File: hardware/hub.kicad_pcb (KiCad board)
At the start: 4 copper layers, 100 x 85 mm, 153 parts, among them J101 USB-A, J102 TNG-Power-BTM, J103 TNG-Power-TOP, J104 TNG-Data-BTM, J105 TNG-Data-TOP, P101 Debug, P102 PE, P202 PWR IN, SW101 BOOT, T201 744272251, U101 USB2517, U102 MIC2026-1YM, U103 82400152, U104 STM32F070CBT6, U105 TPD4S010DQA, U106 TPD4S010DQA, U107 TPD4S010DQA, U110 TPS22975, U112 VN7140AS, U201 AZ1117EH, U203 BD90640HFP, U204 PAC1933, X101 24MHz, X102 8MHz

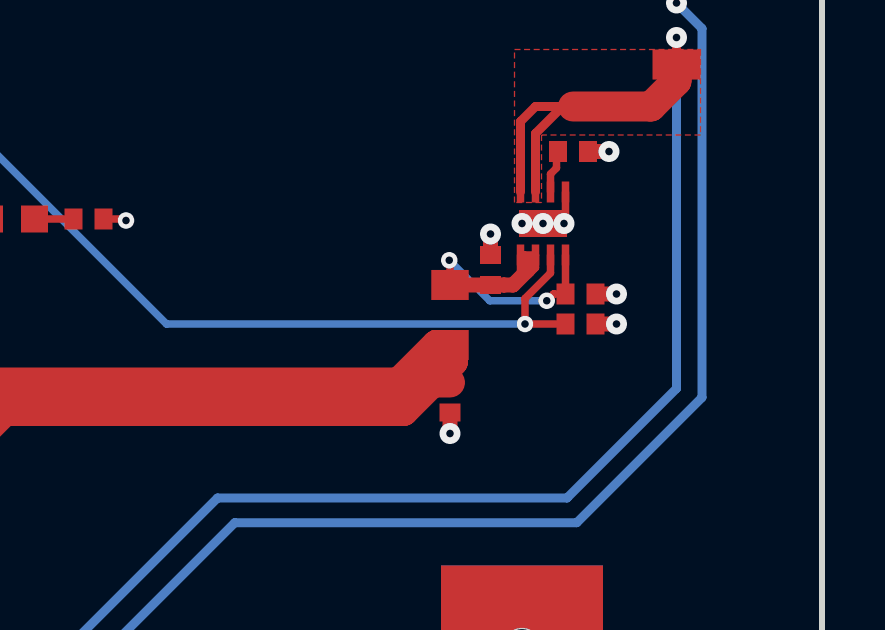
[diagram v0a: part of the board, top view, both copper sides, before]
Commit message: fix footprint
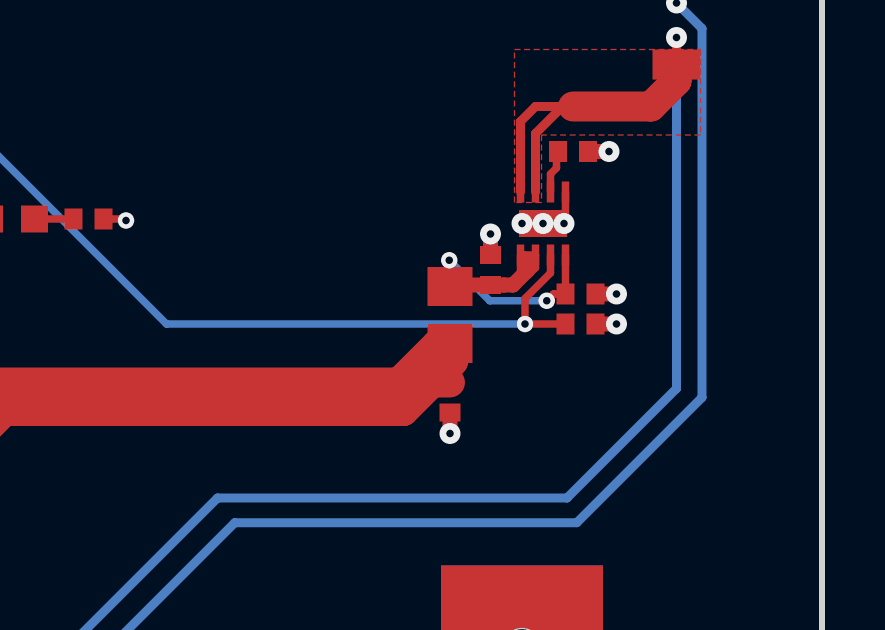
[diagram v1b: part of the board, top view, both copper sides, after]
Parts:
- L109: footprint kicad-libraries:R0805 -> kicad-libraries:R0805E

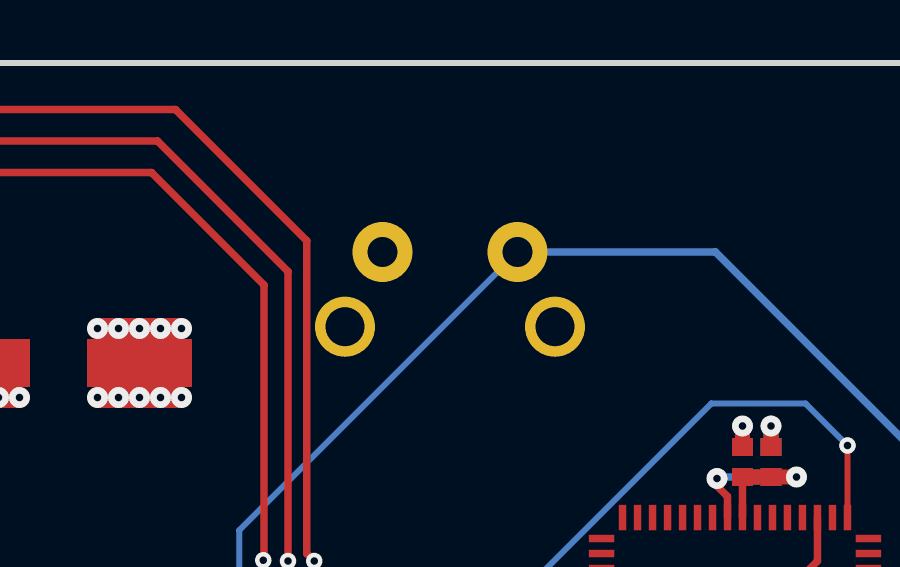
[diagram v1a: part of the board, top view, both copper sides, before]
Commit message: update all footprints
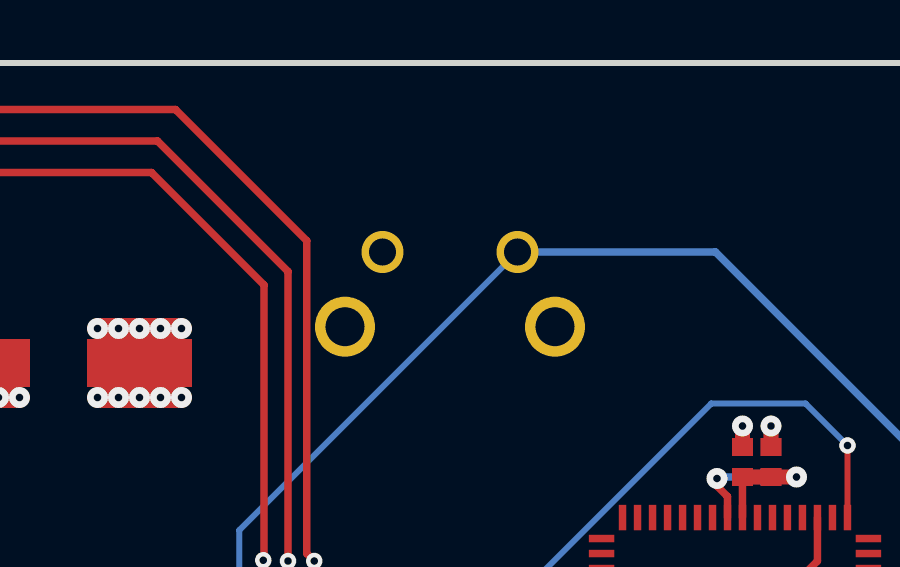
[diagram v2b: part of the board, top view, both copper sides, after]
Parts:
- C101, C102, C103, C104, C105, C106, C107, C110, C111, C112, C113, C114, C115, C116, C118, C119, C121, C122, C123, C124, C125, C126, C127, C128, C129, C130, C131, C132, C133, C134, C137, C138, C209, C214, C221, C222, C226: footprint C0402F -> kicad-libraries:C0402F
- C108, C109, C117: footprint ELKO_63 -> kicad-libraries:ELKO_63
- C120, C210, C217: footprint C0603F -> kicad-libraries:C0603F
- C201, C202, C204, C206, C207, C211, C227: footprint C1206 -> kicad-libraries:C1206
- D101: footprint LED-LP -> kicad-libraries:LED-LP
- D102: footprint D0603F -> kicad-libraries:D0603F
- D205, D206: footprint SOD-128 -> kicad-libraries:SOD-128
- J102, J104: footprint TNG-40-BTM -> kicad-libraries:TNG-40-BTM
- J103, J105: footprint TNG-40-TOP -> kicad-libraries:TNG-40-TOP
- L101, L108, L201, R208, R212, R214, R215: footprint R0603F -> kicad-libraries:R0603F
- L102, L103, L104, L105, L106, L107, L110: footprint WE-CNSW-0603 -> kicad-libraries:WE-CNSW-0603
- L202: footprint WE-LHMI -> kicad-libraries:WE-LHMI
- L203: footprint SRP7030 -> kicad-libraries:SRP7030
- LED101: footprint LED-RGB-LP -> kicad-libraries:LED-RGB-LP
- P202: footprint OQ_4P -> kicad-libraries:OQ_4P
- R101, R102, R103, R104, R105, R106, R107, R108, R109, R110, R111, R112, R113, R114, R115, R116, R117, R119, R120, R121, R218: footprint R0402F -> kicad-libraries:R0402F
- R204, R206, R207, R209, R219, R220, R221: footprint R1206 -> kicad-libraries:R1206
- T201: footprint WE-SL5 -> kicad-libraries:WE-SL5
- U103: footprint SOT563-SPEC -> kicad-libraries:SOT563-SPEC
- U105, U106, U107: footprint TPD4S010DQA -> kicad-libraries:TPD4S010DQA
- U110: footprint WSON8-2x2 -> kicad-libraries:WSON8-2x2
- U203: footprint BD906XX-C-HRP7 -> kicad-libraries:BD906XX-C-HRP7
- X101: footprint CRYSTAL_3225 -> kicad-libraries:CRYSTAL_3225
